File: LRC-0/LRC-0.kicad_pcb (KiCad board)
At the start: 4 copper layers, 100 x 38.6 mm, 63 parts, among them J1 USB_C_Receptacle_USB2.0_14P, J2 Battery, J3 Conn_01x10, J4 SMA, J5 u.FL, SW1 EN, SW2 BOOT, U1 AP7361C-33E, U2 TVS1400DRV, U3 BQ24075RGT, U4 ESP32-C6-MINI-1, U5 SX1262IMLTRT, U6 RFSW1012TR7, U7 RFSW1012TR7, Y1 TX32-33015S-32.000-X-R

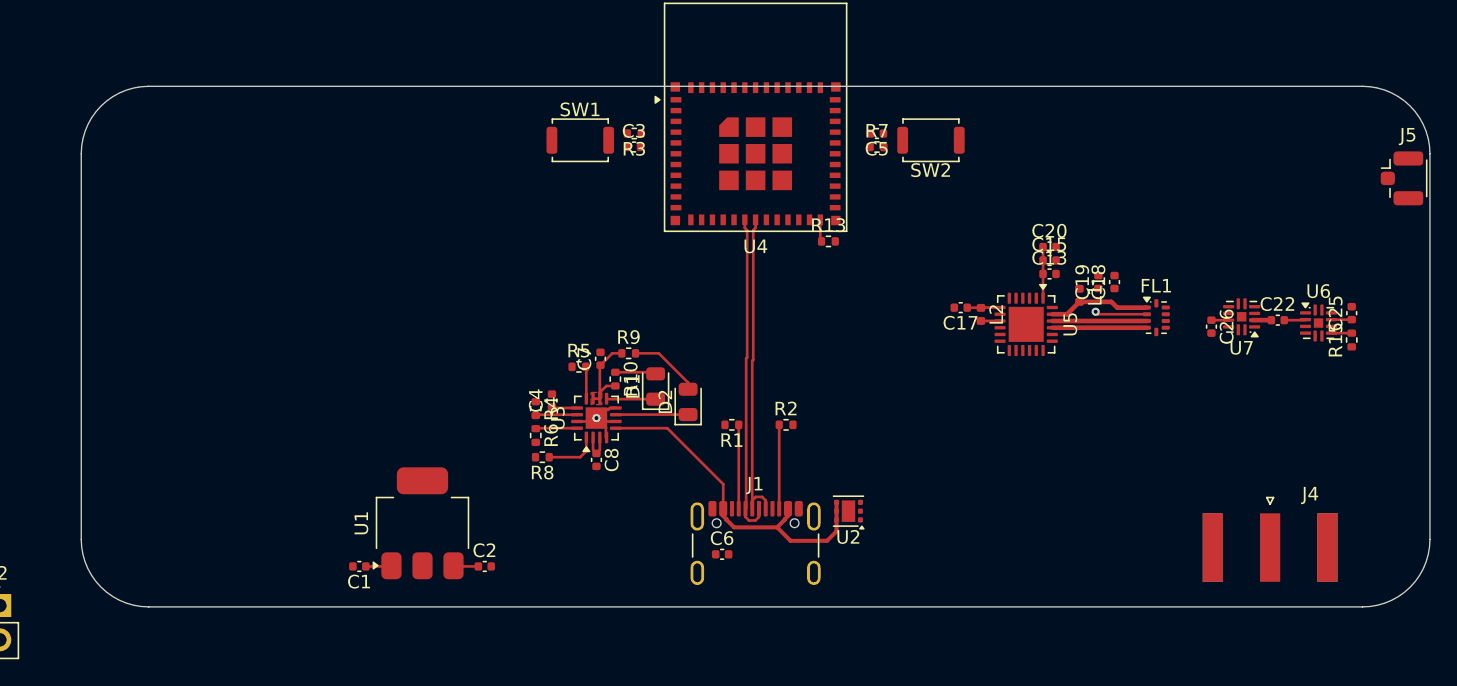
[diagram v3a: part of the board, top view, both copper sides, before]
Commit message: new RF switch for pin side conflict + ground fill for some ICs
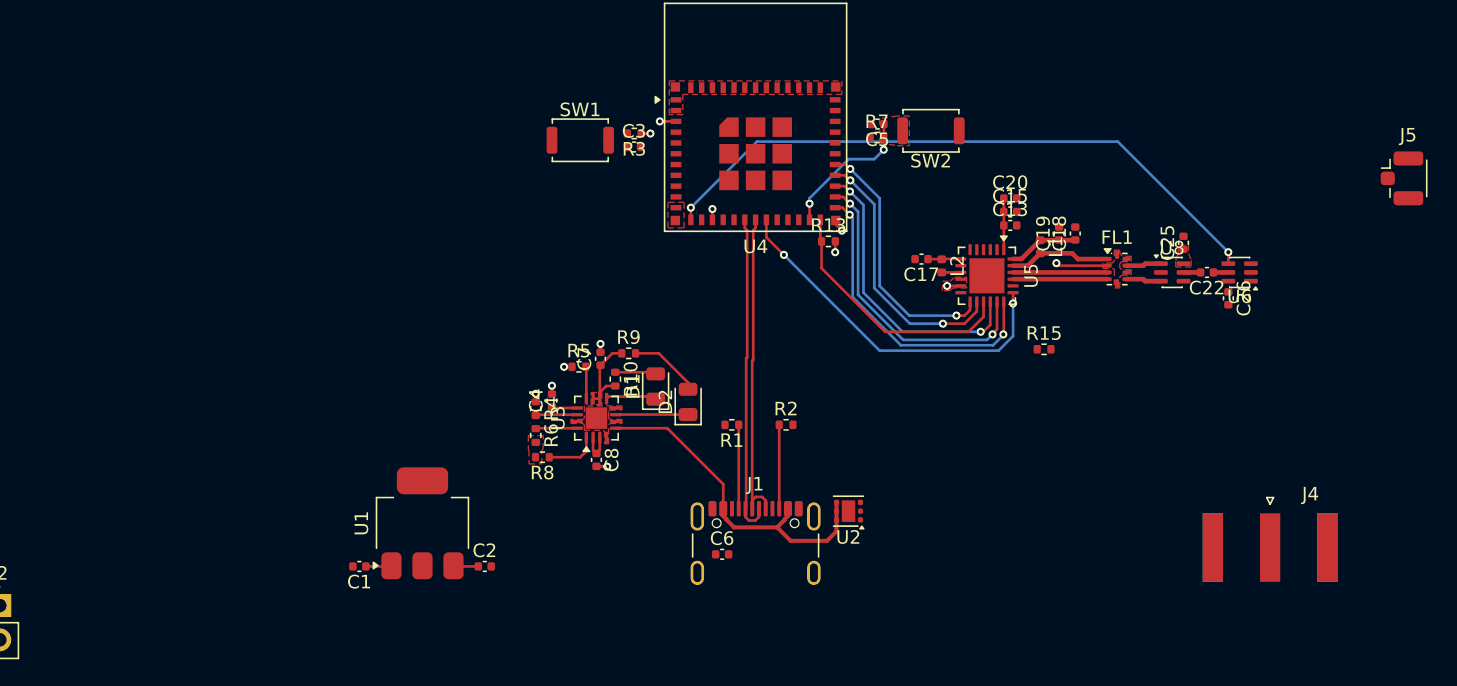
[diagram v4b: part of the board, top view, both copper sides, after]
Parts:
- removed U7: RFSW1012TR7, Package_DFN_QFN:LQFN-12-1EP_2x2mm_P0.5mm_EP0.7x0.7mm
- added U8: 4259-63, Package_TO_SOT_SMD:SOT-363_SC-70-6, F.Cu at (180.9, 108.8)
- U6: value RFSW1012TR7 -> 4259-63; footprint Package_DFN_QFN:LQFN-12-1EP_2x2mm_P0.5mm_EP0.7x0.7mm -> Package_TO_SOT_SMD:SOT-363_SC-70-6
- moved R15 22.8 mm to (171.4, 114.5), turned to 0 degrees
- moved C25 13.5 mm to (181.7, 106.6)
- moved U6 6.95 mm to (185.9, 108.8), turned to 180 degrees
- moved C22 6.33 mm to (183.5, 108.8), turned to 180 degrees
- moved C18 4.63 mm to (173.7, 105.9)
- moved C19 4.63 mm to (172.5, 105.9)
- moved FL1 4.63 mm to (176.8, 108.5)
- moved L1 4.63 mm to (171.1, 106.9)
- moved U5 4.63 mm to (167.2, 109.0)
- moved C13 4.63 mm to (168.9, 105.3)
- moved C15 4.63 mm to (168.9, 104.3)
- moved C17 4.63 mm to (162.3, 107.8)
- moved C20 4.63 mm to (168.9, 103.3)
- moved L2 4.63 mm to (163.8, 108.3)
- moved C26 2.45 mm to (185.1, 110.7)
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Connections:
- C22 pad 2: Net-(U6-RFC) -> Net-(U8-RFC)
- R15 pad 2: Net-(U6-CTRL) -> Net-(U8-CTRL)
- U4 pad 19: /BUSY -> /NSS
- U4 pad 25: /DIO1 -> /SCK
- U4 pad 26: /SCK -> /MOSI
- U4 pad 28: /MOSI -> /BUSY
- U4 pad 29: /NSS -> /DIO1
- U6 pad 1: GND -> /ANT2
- U6 pad 2: Net-(U6-RFC) -> GND
- U6 pad 3: GND -> /ANT1
- U6 pad 4: GND -> /ANT_CTRL
- U6 pad 5: /RF1 -> /RFIN_A
- U6 pad 6: GND -> +3V3
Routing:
- net /ANT_CTRL: track 0.00 -> 47.0 mm, vias 0 -> 2
- net /NSS: track 0.00 -> 26.7 mm, vias 0 -> 2
- net /SCK: track 0.00 -> 22.9 mm, vias 0 -> 2
- net /MOSI: track 0.00 -> 22.4 mm, vias 0 -> 2
- net /MISO: track 0.00 -> 21.7 mm, vias 0 -> 2
- net /BUSY: track 0.00 -> 19.8 mm, vias 0 -> 2
- net /DIO1: track 0.00 -> 19.2 mm, vias 0 -> 2
- net /NRESET: track 1.64 -> 19.2 mm
- net Net-(U4-IO9): track 0.00 -> 10.5 mm, vias 0 -> 2
- net Net-(U5-VR_PA): track 0.03 -> 5.20 mm
- net /RF1: track 0.00 -> 2.61 mm
- net /RF2: track 0.00 -> 2.61 mm
- net Net-(U6-RFC): track 1.58 -> 0.00 mm
- net Net-(U6-CTRL): track 1.50 -> 0.00 mm
- net Net-(U8-RFC): track 0.00 -> 1.26 mm
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- added copper zone on F.Cu, net +3V3
- added copper zone on F.Cu, net GND
- added copper zone on In1.Cu, net GND
- added copper zone on F.Cu, net Net-(U4-IO9)
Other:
- board outline removed

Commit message: rf route for filter and transceiver
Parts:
- removed C14, C16, C21, C24, C27: C, Capacitor_SMD:C_0402_1005Metric
- removed C23: 47n, Capacitor_SMD:C_0402_1005Metric
- removed L3, L4: L, Inductor_SMD:L_0402_1005Metric
- added C12: 10p, Capacitor_SMD:C_0402_1005Metric, F.Cu at (45.2, 18.9)
- added R14: 220, Resistor_SMD:R_0402_1005Metric, F.Cu at (47.3, 18.9)
- H1, H2, H3, H4: value MountingHole_Pad -> MountingHole; footprint MountingHole:MountingHole_3.2mm_M3 -> MountingHole:MountingHole_2.2mm_M2
- L2: footprint Inductor_SMD:L_0402_1005Metric -> Inductor_SMD:L_0603_1608Metric
- U4: footprint RF_Module:ESP32-C6-MINI-1 -> ESP32_C6_MINI_1U_H4:XCVR_ESP32-C6-MINI-1U-H4
- moved J3 270.4 mm to (240.8, 122.9)
- moved H1 238.2 mm to (246.1, 135.8)
- moved H2 237.3 mm to (246.1, 141.7)
- moved H3 236.3 mm to (246.1, 147.7)
- moved H4 235.3 mm to (246.1, 153.6)
- moved J1 180.4 mm to (3.40, 24.8), turned to -90 degrees
- moved SW2 179.3 mm to (7.72, 8.60), turned to 0 degrees
- moved J2 176.5 mm to (270.0, 146.9)
- moved C5 173.3 mm to (11.4, 7.08), turned to 90 degrees
- moved R7 172.8 mm to (11.4, 9.11), turned to 90 degrees
- moved R15 164.7 mm to (40.1, 15.0), turned to 90 degrees
- moved FL1 159.1 mm to (41.9, 24.2), turned to -90 degrees
- moved U4 157.4 mm to (19.8, 11.6)
- moved C3 155.6 mm to (11.2, 13.7), turned to -90 degrees
- moved U8 155.3 mm to (47.9, 28.5)
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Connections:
- Y1 pad 3: Net-(Y1-OUTPUT) -> Net-(Y1-VDC)
- Y1 pad 4: Net-(Y1-VDC) -> Net-(Y1-OUTPUT)
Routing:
- net /ANT_CTRL: track 47.0 -> 1.50 mm, vias 2 -> 1
- net Net-(U8-CTRL): track 0.00 -> 32.4 mm, vias 0 -> 2
- net +5V: track 27.3 -> 0.00 mm
- net GND: track 9.28 -> 23.3 mm, vias 8 -> 9
- net Net-(U4-IO9): track 10.5 -> 22.4 mm
- net VCC: track 8.68 -> 0.00 mm
- net /SCK: track 22.9 -> 15.5 mm, vias 2 -> 0
- net /MOSI: track 22.4 -> 15.6 mm, vias 2 -> 0
- net /RF1: track 2.61 -> 9.36 mm
- net Net-(J1-CC2): track 6.22 -> 0.00 mm
- net Net-(J1-CC1): track 6.22 -> 0.00 mm
- net /MISO: track 21.7 -> 15.8 mm, vias 2 -> 0
- net /D-: track 24.0 -> 18.4 mm
- net /D+: track 24.0 -> 18.5 mm
- net Net-(D2-K): track 5.36 -> 0.00 mm
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- added copper zone on In2.Cu, net +3V3
- removed copper zone on F.Cu, net +3V3
- removed copper zone on F.Cu, net GND
- removed copper zone on F.Cu, net Net-(U4-IO9)
- removed copper zone on F.Cu, net VCC
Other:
- board outline added: 100 x 100 mm

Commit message: switch
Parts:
- moved C25 237.4 mm to (49.2, 26.8)
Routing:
- net +3V3: track 4.83 -> 5.88 mm
- net /RF2: track 6.55 -> 7.26 mm
- net GND: vias 9 -> 18

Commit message: battery charger circuit
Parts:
- moved U2 283.2 mm to (9.69, 28.6), turned to 180 degrees
- moved J2 274.9 mm to (2.75, 82.5), turned to 180 degrees
- moved R1 274.6 mm to (9.25, 22.4), turned to 90 degrees
- moved R2 273.6 mm to (9.31, 26.6)
- moved U1 270.2 mm to (18.5, 33.2), turned to 90 degrees
- moved U3 262.2 mm to (8.50, 77.4)
- moved D2 261.6 mm to (13.2, 82.2)
- moved D1 261.5 mm to (13.2, 80.0)
- moved R8 259.7 mm to (4.74, 76.7), turned to 180 degrees
- moved R6 258.7 mm to (6.00, 74.0), turned to 90 degrees
- moved C1 257.2 mm to (13.8, 33.2), turned to 90 degrees
- moved R4 255.7 mm to (8.25, 73.2), turned to -90 degrees
- moved C8 253.2 mm to (5.50, 80.0)
- moved R5 252.6 mm to (11.2, 76.0), turned to -90 degrees
- moved C2 249.7 mm to (22.8, 33.2), turned to 90 degrees
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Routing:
- net +5V: track 0.00 -> 13.7 mm, vias 0 -> 2
- net +3V3: track 5.88 -> 14.5 mm, vias 2 -> 7
- net VCC: track 0.00 -> 5.72 mm
- net Net-(D2-K): track 0.00 -> 5.16 mm
- net Net-(D1-K): track 0.00 -> 3.06 mm
- net Net-(U8-CTRL): track 32.4 -> 29.4 mm
- net Net-(U3-ISET): track 0.00 -> 2.95 mm
- net Net-(U3-TMR): track 0.00 -> 2.45 mm
- net /D-: track 18.4 -> 20.9 mm
- net /D+: track 18.5 -> 20.9 mm
- net Net-(J1-CC1): track 0.00 -> 2.43 mm
- net /BAT+: track 0.00 -> 2.27 mm
- net Net-(U5-VR_PA): track 1.79 -> 3.86 mm
- net Net-(U3-TS): track 0.00 -> 1.81 mm
- net Net-(J1-CC2): track 0.00 -> 1.73 mm
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- added copper zone on F.Cu, net +3V3
- added copper zone on F.Cu, net GND

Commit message: idk
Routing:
- net +5V: track 13.7 -> 22.5 mm
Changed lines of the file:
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@@
 		(capping no)
 		(filling no)
-		(zone_defaults)
 		(pcbplotparams
 			(layerselection 0x00000000_00000000_55555555_5755f5ff)
@@
 	)
 	(segment
-		(start 9.25 74.75)
-		(end 9.25 76)
+		(start 9.25 73.85)
+		(end 9.95 73.15)
 		(width 0.2)
 		(layer "F.Cu")
@@
 	)
 	(segment
-		(start 6.464594 27.22)
-		(end 7.075 27.22)
+		(start 9.25 74.75)
+		(end 9.25 76)
 		(width 0.2)
 		(layer "F.Cu")
@@
 	)
 	(segment
-		(start 9.25 76)
-		(end 9.8 76)
+		(start 6.464594 27.22)
+		(end 7.075 27.22)
 		(width 0.2)
 		(layer "F.Cu")
@@
 	)
 	(segment
-		(start 9.8 76)
-		(end 10.05 75.75)
-		(width 0.2)
-		(layer "F.Cu")
-		(net "+5V")
-	)
-	(segment
 		(start 5.1 23.820001)
 		(end 5.1 25.855406)
@@
 		(net "+5V")
 	)
+	(segment
+		(start 9.25 74.75)
+		(end 9.25 73.85)
+		(width 0.2)
+		(layer "F.Cu")
+		(net "+5V")
+	)
 	(via
-		(at 10.05 75.75)
+		(at 9.95 73.15)
 		(size 0.6)
 		(drill 0.3)
@@
 	)
 	(segment
+		(start 8.5 77.45)
+		(end 9.25 76.7)
+		(width 0.6)
+		(layer "B.Cu")
+		(net "+5V")
+	)
+	(segment
+		(start 8.5 79.25)
+		(end 8.5 77.45)
+		(width 0.6)
+		(layer "B.Cu")
+		(net "+5V")
+	)
+	(segment
+		(start 9.25 76.7)
+		(end 9.25 73.85)
+		(width 0.6)
+		(layer "B.Cu")
+		(net "+5V")
+	)
+	(segment
+		(start 7.75 80)
+		(end 8.5 79.25)
+		(width 0.6)
+		(layer "B.Cu")
+		(net "+5V")
+	)
+	(segment
+		(start 9.25 73.85)
+		(end 9.95 73.15)
+		(width 0.6)
+		(layer "B.Cu")
+		(net "+5V")
+	)
+	(segment
 		(start 8.75 78.875)
 		(end 8.75 79.326886)
@@
 	)
 	(segment
-		(start 32.2 12.4)
-		(end 37.15 17.35)
+		(start 37.05 17.35)
+		(end 39.4625 17.35)
 		(width 0.2)
 		(layer "F.Cu")
@@
 	)
 	(segment
-		(start 37.15 17.35)
-		(end 39.4625 17.35)
+		(start 32.1 12.4)
+		(end 37.05 17.35)
 		(width 0.2)
 		(layer "F.Cu")
@@
 	(segment
 		(start 25.7 12.4)
-		(end 32.2 12.4)
+		(end 32.1 12.4)
 		(width 0.2)
 		(layer "F.Cu")
